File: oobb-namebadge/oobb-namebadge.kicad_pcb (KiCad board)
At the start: 2 copper layers, 90 x 70 mm, 18 parts, among them J1 Conn_02x03_Row_Letter_First, J2 Conn_02x03_Row_Letter_First, J3 Conn_02x03_Row_Letter_First, J4 Conn_02x03_Row_Letter_First

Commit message: needs lipo charger
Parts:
- added G***: LOGO, oobb:hello-inv, F.Cu at (173.5, 108.5)
- added J6: Conn_02x03_Odd_Even, oobb:Pin_Header_Straight_2x03_Pitch2.54mm, F.Cu at (175.0, 148.5)
- added J7: Conn_01x01, Connectors_TestPoints:Test_Point_Pad_d1.5mm, B.Cu at (168.0, 100.0)
- added J8: Conn_01x01, Connectors_TestPoints:Test_Point_Pad_d1.5mm, B.Cu at (168.0, 104.0)
- J1, J2, J3, J4: value Conn_02x03_Row_Letter_First -> Conn_02x03_Odd_Even; footprint Pin_Headers:Pin_Header_Straight_2x03_Pitch2.54mm -> oobb:Pin_Header_Straight_2x03_Pitch2.54mm
- moved J1 3.81 mm to (141.5, 148.5), turned to 225 degrees
- moved J3 3.63 mm to (208.5, 148.5), turned to 315 degrees
- moved J2 2.12 mm to (141.5, 101.5), turned to 135 degrees
- moved J4 1.78 mm to (208.5, 101.5), turned to 45 degrees
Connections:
- J1 pad 1: (no net) -> GND
- J1 pad 2: (no net) -> +3V3
- J1 pad 3: (no net) -> Net-(J1-Pad3)
- J1 pad 4: (no net) -> Net-(J1-Pad4)
- J1 pad 5: (no net) -> Net-(J1-Pad5)
- J1 pad 6: (no net) -> Net-(J1-Pad6)
- J2 pad 1: (no net) -> GND
- J2 pad 2: (no net) -> +3V3
- J2 pad 3: (no net) -> Net-(J2-Pad3)
- J2 pad 4: (no net) -> Net-(J2-Pad4)
- J2 pad 5: (no net) -> Net-(J2-Pad5)
- J2 pad 6: (no net) -> Net-(J2-Pad6)
- J3 pad 1: (no net) -> GND
- J3 pad 2: (no net) -> +3V3
- J3 pad 3: (no net) -> Net-(J3-Pad3)
- J3 pad 4: (no net) -> Net-(J3-Pad4)
- J3 pad 5: (no net) -> Net-(J3-Pad5)
- J3 pad 6: (no net) -> Net-(J3-Pad6)
- J4 pad 1: (no net) -> GND
- J4 pad 2: (no net) -> +3V3
- J4 pad 3: (no net) -> Net-(J4-Pad3)
- J4 pad 4: (no net) -> Net-(J4-Pad4)
- J4 pad 5: (no net) -> Net-(J4-Pad5)
- J4 pad 6: (no net) -> Net-(J4-Pad6)
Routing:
- net +3V3: track 0.00 -> 196.2 mm
- added copper zone on B.Cu, net GND
- added copper zone on F.Cu, net GND
- removed copper zone on F.Cu, net (none)
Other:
- net class power added: clearance 0.3, trace_width 0.3, via_dia 0.8, via_drill 0.4
- board text added: "Matt Venn 2019"
- board text removed: "Hello my name is"
- board text removed: "Stuart is a massive bellend"

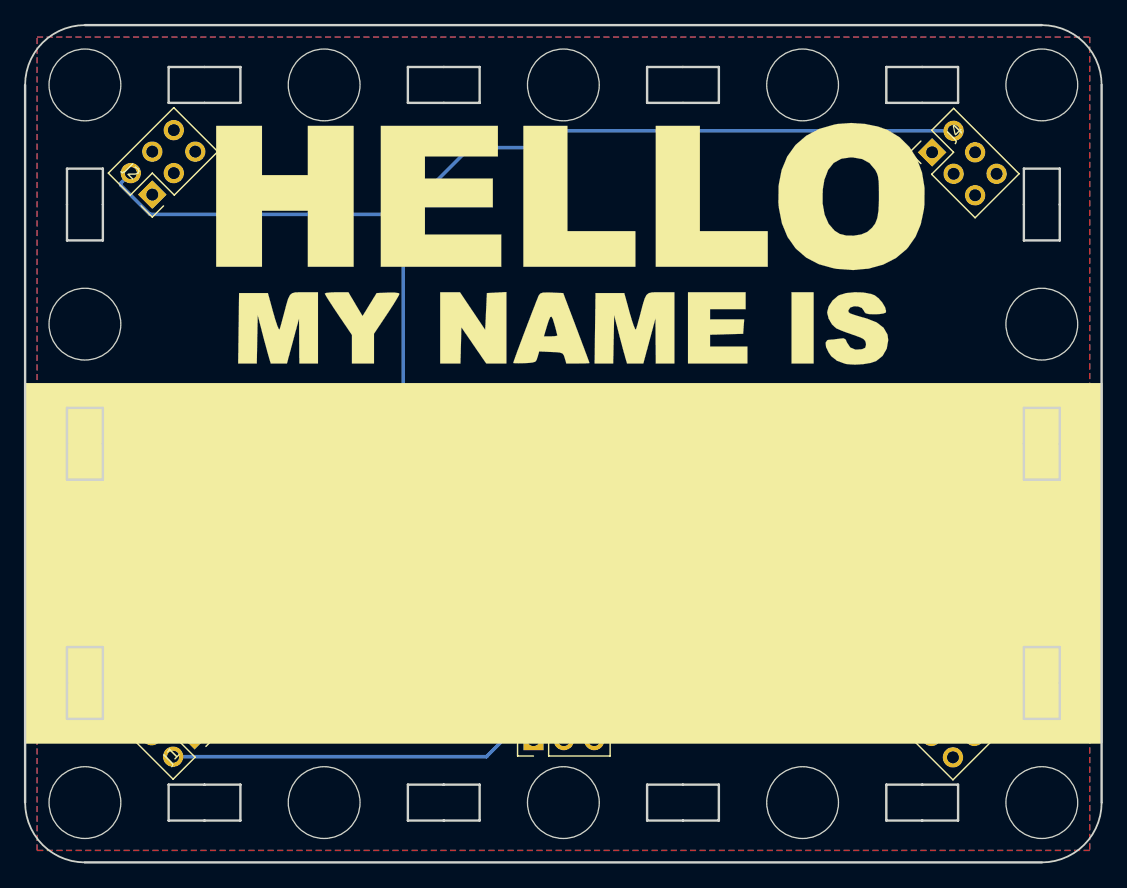
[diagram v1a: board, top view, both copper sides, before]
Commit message: added icebreaker, ldo, switch and boost board
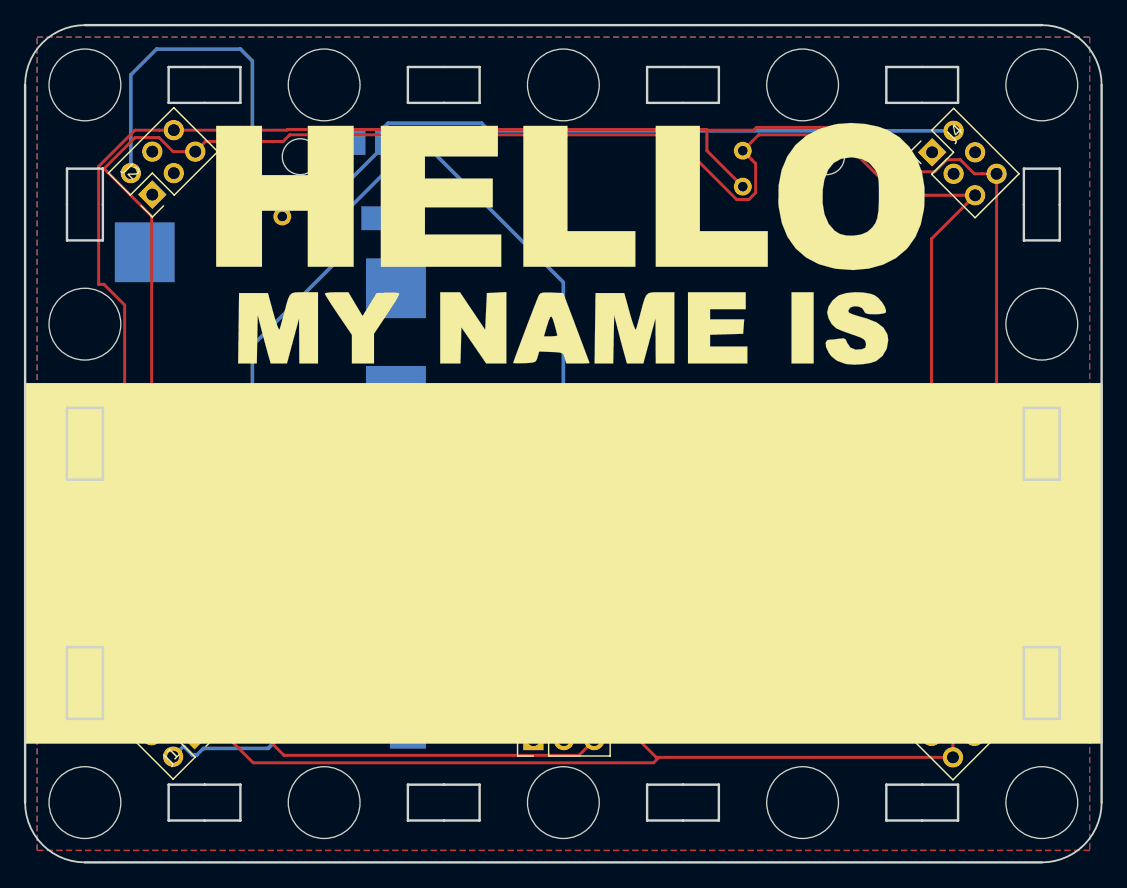
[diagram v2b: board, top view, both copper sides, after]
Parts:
- added J5: Conn_01x06, oobb:icebreaker, F.Cu at (200.0, 135.0)
- added SW1: SW_SPDT, Buttons_Switches_SMD:SW_SPDT_CK-JS102011SAQN, B.Cu at (154.0, 147.0)
- added U1: AP1117-15, TO_SOT_Packages_SMD:SOT-223, B.Cu at (160.0, 103.0)
- added U2: lipo-charger-boost, oobb:lipo-charger-boost, B.Cu at (139.0, 108.0)
- J7, J8: footprint Connectors_TestPoints:Test_Point_Pad_d1.5mm -> Measurement_Points:Measurement_Point_Square-SMD-Pad_Big
- moved J7 49.4 mm to (162.0, 149.0)
- moved J8 40.4 mm to (162.0, 144.0)
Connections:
- J1 pad 3: Net-(J1-Pad3) -> /scl
- J1 pad 4: Net-(J1-Pad4) -> /sda
- J1 pad 5: Net-(J1-Pad5) -> /gpio2
- J1 pad 6: Net-(J1-Pad6) -> /gpio1
- J2 pad 3: Net-(J2-Pad3) -> /scl
- J2 pad 4: Net-(J2-Pad4) -> /sda
- J2 pad 5: Net-(J2-Pad5) -> /gpio2
- J2 pad 6: Net-(J2-Pad6) -> /gpio1
- J3 pad 3: Net-(J3-Pad3) -> /scl
- J3 pad 4: Net-(J3-Pad4) -> /sda
- J3 pad 5: Net-(J3-Pad5) -> /gpio2
- J3 pad 6: Net-(J3-Pad6) -> /gpio1
- J4 pad 3: Net-(J4-Pad3) -> /scl
- J4 pad 4: Net-(J4-Pad4) -> /sda
- J4 pad 5: Net-(J4-Pad5) -> /gpio2
- J4 pad 6: Net-(J4-Pad6) -> /gpio1
- J6 pad 3: Net-(J6-Pad3) -> /scl
- J6 pad 4: Net-(J6-Pad4) -> /sda
- J6 pad 5: Net-(J6-Pad5) -> /gpio2
- J6 pad 6: Net-(J6-Pad6) -> /gpio1
- J7 pad 1: +3V3 -> /lipo
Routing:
- net /gpio1: track 0.00 -> 262.0 mm
- net /gpio2: track 0.00 -> 251.7 mm
- net /boost-out: track 0.00 -> 87.1 mm
- net Net-(SW1-Pad2): track 0.00 -> 26.1 mm
- net +3V3: track 196.2 -> 173.4 mm
- net /lipo: track 0.00 -> 7.57 mm
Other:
- board text added: "gnd"
- board text added: "lipo"
- board text added: "lipo+"

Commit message: fp files
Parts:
- moved U2 2.06 mm to (141.0, 108.5)
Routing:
- net +3V3: track 173.4 -> 218.6 mm
- net /boost-out: track 87.1 -> 89.4 mm
- net /gpio2: track 251.7 -> 253.3 mm
- net /gpio1: track 262.0 -> 260.9 mm
- net Net-(SW1-Pad2): track 26.1 -> 27.2 mm

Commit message: ready to fab
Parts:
- added R1: 10k, Resistors_SMD:R_0805_HandSoldering, B.Cu at (147.6, 104.2)
- added R2: 10k, Resistors_SMD:R_0805_HandSoldering, B.Cu at (147.6, 106.6)
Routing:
- net /gpio1: track 260.9 -> 271.3 mm
- net /gpio2: track 253.3 -> 263.7 mm
- net +3V3: track 218.6 -> 223.1 mm
- net Net-(SW1-Pad2): track 27.2 -> 25.6 mm
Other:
- net class Default: clearance 0.2 -> 0.22
- net class power: trace_width 0.3 -> 0.5; via_dia 0.8 -> 0.9; via_drill 0.4 -> 0.5
- rule trace_clearance: 0.2 -> 0.22
- board text added: "$ver$"
- board text added: "3.3"
- board text added: "J5019 lipo charger & boost module"
- board text added: "boost out"
- board text added: "in compliance with SAO V.1.69bis"
